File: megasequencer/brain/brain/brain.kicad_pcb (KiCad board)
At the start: 2 copper layers, 99.1 x 99.1 mm, 90 parts, among them J1 TOP, J2 BOTTOM, J3 Keyboard, J4 EURO_PWR_2x5, J5 ICSP, J6 TO_OUTPUTS, J7 FROM_OUTPUTS, J8 RIGHT, SW1 RST, U1 78L05, U2 ATmega328P-PU, U3 TL074, U4 TL072, U5 74HC595, U6 74HC595, U7 TL074, U8 TL074, Y1 Crystal

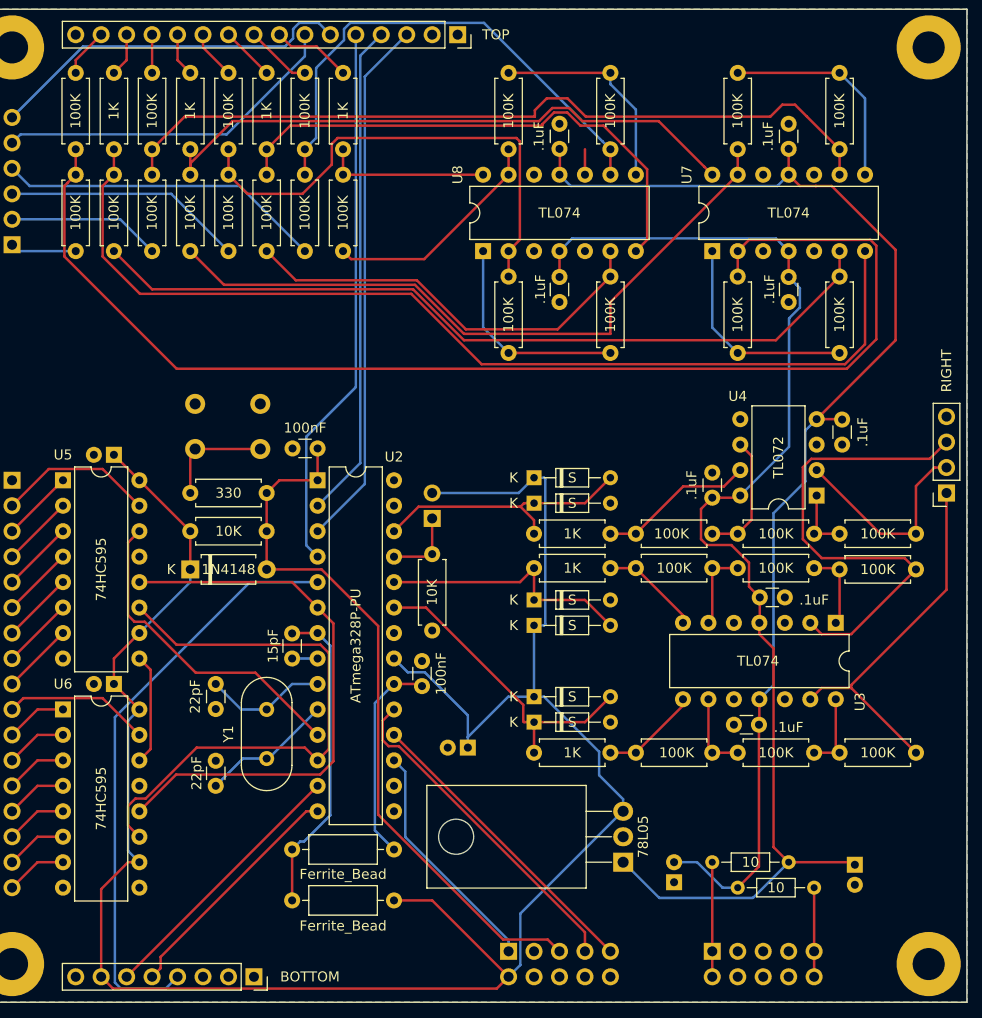
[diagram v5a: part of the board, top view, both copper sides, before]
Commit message: Finish up labeling and fixa connector that was in the wrong direction
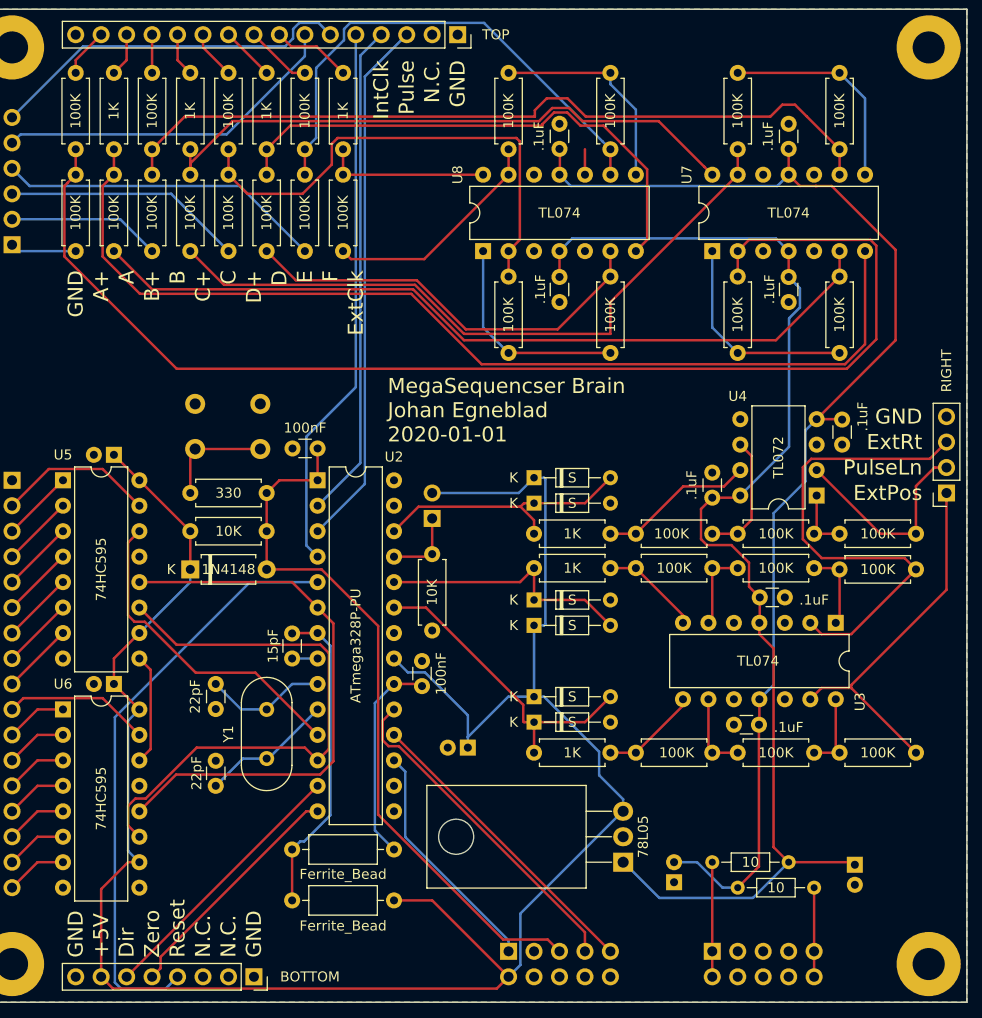
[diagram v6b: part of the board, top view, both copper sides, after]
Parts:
- J4: value EURO_PWR_2x5 -> POWER
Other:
- board text added: "+5V"
- board text added: "10"
- board text added: "11"
- board text added: "12"
- board text added: "13"
- board text added: "14"
- board text added: "15"
- board text added: "16"
- board text added: "2"
- board text added: "3"
- board text added: "4"
- board text added: "5"
- board text added: "6"
- board text added: "7"
- board text added: "8"
- board text added: "9"
- board text added: "A"
- board text added: "A+"
- board text added: "B"
- board text added: "B+"
- board text added: "C"
- board text added: "C+"
- board text added: "D"
- board text added: "D+"
- board text added: "Dir"
- board text added: "E"
- board text added: "ExtClk"
- board text added: "ExtPos"
- board text added: "ExtRt"
- board text added: "F"
- board text added: "G"
- board text added: "GND"
- board text added: "IntClk"
- board text added: "MegaSequencser Brain Johan Egneblad 2020-01-01"
- board text added: "N.C."
- board text added: "Pulse"
- board text added: "PulseLn"
- board text added: "Reset"
- board text added: "Zero"
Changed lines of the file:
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@@
   (general
     (thickness 1.6)
-    (drawings 7)
+    (drawings 59)
     (tracks 458)
     (zones 0)
@@
   (page A4)
   (layers
-    (0 F.Cu signal hide)
-    (31 B.Cu signal hide)
+    (0 F.Cu signal)
+    (31 B.Cu signal)
     (32 B.Adhes user)
     (33 F.Adhes user)
@@
       (effects (font (size 1 1) (thickness 0.15)) (justify mirror))
     )
-    (fp_text value EURO_PWR_2x5 (at -3.175 -6.35) (layer B.SilkS)
+    (fp_text value POWER (at -3.175 -9.525) (layer B.SilkS)
       (effects (font (size 1 1) (thickness 0.15)) (justify mirror))
     )
@@
       (effects (font (size 1 1) (thickness 0.15)))
     )
-    (fp_text value .1uF (at 1.25 2.05 90) (layer F.SilkS)
+    (fp_text value .1uF (at 2.794 2.05 90) (layer F.SilkS)
       (effects (font (size 1 1) (thickness 0.15)))
     )
@@
     )
   )
+  (gr_text 16 (at 31.115 113.03) (layer B.SilkS)
+    (effects (font (size 1 1) (thickness 0.15)) (justify right mirror))
+  )
+  (gr_text 15 (at 31.115 110.49) (layer B.SilkS)
+    (effects (font (size 1 1) (thickness 0.15)) (justify right mirror))
+  )
+  (gr_text 14 (at 31.115 107.95) (layer B.SilkS)
+    (effects (font (size 1 1) (thickness 0.15)) (justify right mirror))
+  )
+  (gr_text 13 (at 31.115 105.41) (layer B.SilkS)
+    (effects (font (size 1 1) (thickness 0.15)) (justify right mirror))
+  )
+  (gr_text 12 (at 31.115 102.87) (layer B.SilkS)
+    (effects (font (size 1 1) (thickness 0.15)) (justify right mirror))
+  )
+  (gr_text 11 (at 31.115 100.33) (layer B.SilkS)
+    (effects (font (size 1 1) (thickness 0.15)) (justify right mirror))
+  )
+  (gr_text 10 (at 31.115 97.79) (layer B.SilkS)
+    (effects (font (size 1 1) (thickness 0.15)) (justify right mirror))
+  )
+  (gr_text 9 (at 31.75 95.25) (layer B.SilkS)
+    (effects (font (size 1 1) (thickness 0.15)) (justify right mirror))
+  )
+  (gr_text 8 (at 31.75 92.71) (layer B.SilkS)
+    (effects (font (size 1 1) (thickness 0.15)) (justify right mirror))
+  )
+  (gr_text 7 (at 31.75 90.17) (layer B.SilkS)
+    (effects (font (size 1 1) (thickness 0.15)) (justify right mirror))
+  )
+  (gr_text 6 (at 31.75 87.63) (layer B.SilkS)
+    (effects (font (size 1 1) (thickness 0.15)) (justify right mirror))
+  )
+  (gr_text 5 (at 31.75 85.09) (layer B.SilkS)
+    (effects (font (size 1 1) (thickness 0.15)) (justify right mirror))
+  )
+  (gr_text 4 (at 31.75 82.55) (layer B.SilkS)
+    (effects (font (size 1 1) (thickness 0.15)) (justify right mirror))
+  )
+  (gr_text 3 (at 31.75 80.01) (layer B.SilkS)
+    (effects (font (size 1 1) (thickness 0.15)) (justify right mirror))
+  )
+  (gr_text 2 (at 31.75 77.47) (layer B.SilkS)
+    (effects (font (size 1 1) (thickness 0.15)) (justify right mirror))
+  )
+  (gr_text 1 (at 31.75 74.93) (layer B.SilkS)
+    (effects (font (size 1 1) (thickness 0.15)) (justify right mirror))
+  )
+  (gr_text G (at 31.75 72.39) (layer B.SilkS)
+    (effects (font (size 1 1) (thickness 0.15)) (justify right mirror))
+  )
+  (gr_text F (at 31.75 36.195) (layer B.SilkS)
+    (effects (font (size 1 1) (thickness 0.15)) (justify right mirror))
+  )
+  (gr_text E (at 31.75 38.735) (layer B.SilkS)
+    (effects (font (size 1 1) (thickness 0.15)) (justify right mirror))
+  )
+  (gr_text D (at 31.75 41.275) (layer B.SilkS)
+    (effects (font (size 1 1) (thickness 0.15)) (justify right mirror))
+  )
+  (gr_text C (at 31.75 43.815) (layer B.SilkS)
+    (effects (font (size 1 1) (thickness 0.15)) (justify right mirror))
+  )
+  (gr_text B (at 31.75 46.355) (layer B.SilkS)
+    (effects (font (size 1 1) (thickness 0.15)) (justify right mirror))
+  )
+  (gr_text A (at 31.75 48.895) (layer B.SilkS)
+    (effects (font (size 1 1) (thickness 0.15)) (justify right mirror))
+  )
+  (gr_text "MegaSequencser Brain\nJohan Egneblad\n2020-01-01" (at 66.675 65.405) (layer F.SilkS)
+    (effects (font (size 1.5 1.5) (thickness 0.3)) (justify left))
+  )
+  (gr_text GND (at 120.015 66.04) (layer F.SilkS)
+    (effects (font (size 1.5 1.5) (thickness 0.3)) (justify right))
+  )
+  (gr_text ExtRt (at 120.015 68.58) (layer F.SilkS)
+    (effects (font (size 1.5 1.5) (thickness 0.3)) (justify right))
+  )
+  (gr_text PulseLn (at 120.015 71.12) (layer F.SilkS)
+    (effects (font (size 1.5 1.5) (thickness 0.3)) (justify right))
+  )
+  (gr_text ExtPos (at 120.015 73.66) (layer F.SilkS)
+    (effects (font (size 1.5 1.5) (thickness 0.3)) (justify right))
+  )
+  (gr_text GND (at 53.34 120.015 90) (layer F.SilkS)
+    (effects (font (size 1.5 1.5) (thickness 0.3)) (justify left))
+  )
+  (gr_text N.C. (at 50.8 120.015 90) (layer F.SilkS)
+    (effects (font (size 1.5 1.5) (thickness 0.3)) (justify left))
+  )
+  (gr_text N.C. (at 48.26 120.015 90) (layer F.SilkS)
+    (effects (font (size 1.5 1.5) (thickness 0.3)) (justify left))
+  )
+  (gr_text Reset (at 45.72 120.015 90) (layer F.SilkS)
+    (effects (font (size 1.5 1.5) (thickness 0.3)) (justify left))
+  )
+  (gr_text Zero (at 43.18 120.015 90) (layer F.SilkS)
+    (effects (font (size 1.5 1.5) (thickness 0.3)) (justify left))
+  )
+  (gr_text Dir (at 40.64 120.015 90) (layer F.SilkS)
+    (effects (font (size 1.5 1.5) (thickness 0.3)) (justify left))
+  )
+  (gr_text +5V (at 38.1 120.015 90) (layer F.SilkS)
+    (effects (font (size 1.5 1.5) (thickness 0.3)) (justify left))
+  )
+  (gr_text GND (at 35.56 120.015 90) (layer F.SilkS)
+    (effects (font (size 1.5 1.5) (thickness 0.3)) (justify left))
+  )
+  (gr_text GND (at 73.66 30.48 90) (layer F.SilkS)
+    (effects (font (size 1.5 1.5) (thickness 0.3)) (justify right))
+  )
+  (gr_text N.C. (at 71.12 30.48 90) (layer F.SilkS)
+    (effects (font (size 1.5 1.5) (thickness 0.3)) (justify right))
+  )
+  (gr_text Pulse (at 68.58 30.48 90) (layer F.SilkS)
+    (effects (font (size 1.5 1.5) (thickness 0.3)) (justify right))
+  )
+  (gr_text IntClk (at 66.04 30.48 90) (layer F.SilkS)
+    (effects (font (size 1.5 1.5) (thickness 0.3)) (justify right))
+  )
+  (gr_text ExtClk (at 63.5 51.435 90) (layer F.SilkS)
+    (effects (font (size 1.5 1.5) (thickness 0.3)) (justify right))
+  )
+  (gr_text F (at 60.96 51.435 90) (layer F.SilkS)
+    (effects (font (size 1.5 1.5) (thickness 0.3)) (justify right))
+  )
+  (gr_text E (at 58.42 51.435 90) (layer F.SilkS)
+    (effects (font (size 1.5 1.5) (thickness 0.3)) (justify right))
+  )
+  (gr_text D (at 55.88 51.435 90) (layer F.SilkS)
+    (effects (font (size 1.5 1.5) (thickness 0.3)) (justify right))
+  )
+  (gr_text D+ (at 53.34 51.435 90) (layer F.SilkS)
+    (effects (font (size 1.5 1.5) (thickness 0.3)) (justify right))
+  )
+  (gr_text C (at 50.8 51.435 90) (layer F.SilkS)
+    (effects (font (size 1.5 1.5) (thickness 0.3)) (justify right))
+  )
+  (gr_text C+ (at 48.26 51.435 90) (layer F.SilkS)
+    (effects (font (size 1.5 1.5) (thickness 0.3)) (justify right))
+  )
+  (gr_text B (at 45.72 51.435 90) (layer F.SilkS)
+    (effects (font (size 1.5 1.5) (thickness 0.3)) (justify right))
+  )
+  (gr_text B+ (at 43.18 51.435 90) (layer F.SilkS)
+    (effects (font (size 1.5 1.5) (thickness 0.3)) (justify right))
+  )
+  (gr_text A (at 40.64 51.435 90) (layer F.SilkS)
+    (effects (font (size 1.5 1.5) (thickness 0.3)) (justify right))
+  )
+  (gr_text A+ (at 38.1 51.435 90) (layer F.SilkS)
+    (effects (font (size 1.5 1.5) (thickness 0.3)) (justify right))
+  )
+  (gr_text GND (at 35.56 51.435 90) (layer F.SilkS)
+    (effects (font (size 1.5 1.5) (thickness 0.3)) (justify right))
+  )
   (gr_text -12V (at 114.935 120.65 90) (layer B.SilkS)
     (effects (font (size 1 1) (thickness 0.2)) (justify mirror))
@@
   (segment (start 35.56 30.48) (end 35.56 31.75) (width 0.25) (layer F.Cu) (net 32) (status 20))
   (segment (start 38.1 27.94) (end 35.56 30.48) (width 0.25) (layer F.Cu) (net 32) (status 10))
-  (segment (start 40.64 30.48) (end 39.37 31.75) (width 0.25) (layer F.Cu) (net 93) (status 20))
-  (segment (start 40.64 27.94) (end 40.64 30.48) (width 0.25) (layer F.Cu) (net 93) (status 10))
   (segment (start 43.18 27.94) (end 43.18 31.75) (width 0.25) (layer F.Cu) (net 33) (status 30))
   (segment (start 45.72 30.48) (end 46.99 31.75) (width 0.25) (layer F.Cu) (net 34) (status 20))
@@
   (segment (start 46.99 73.66) (end 46.99 69.755) (width 0.25) (layer F.Cu) (net 92) (status 30))
   (segment (start 47.475 69.27) (end 53.975 69.27) (width 0.25) (layer F.Cu) (net 92) (status 30))
+  (segment (start 40.64 30.48) (end 39.37 31.75) (width 0.25) (layer F.Cu) (net 93) (status 20))
+  (segment (start 40.64 27.94) (end 40.64 30.48) (width 0.25) (layer F.Cu) (net 93) (status 10))
   (segment (start 109.964001 87.739001) (end 108.839 86.614) (width 0.25) (layer F.Cu) (net 95) (status 20))
   (segment (start 112.920999 87.739001) (end 109.964001 87.739001) (width 0.25) (layer F.Cu) (net 95))

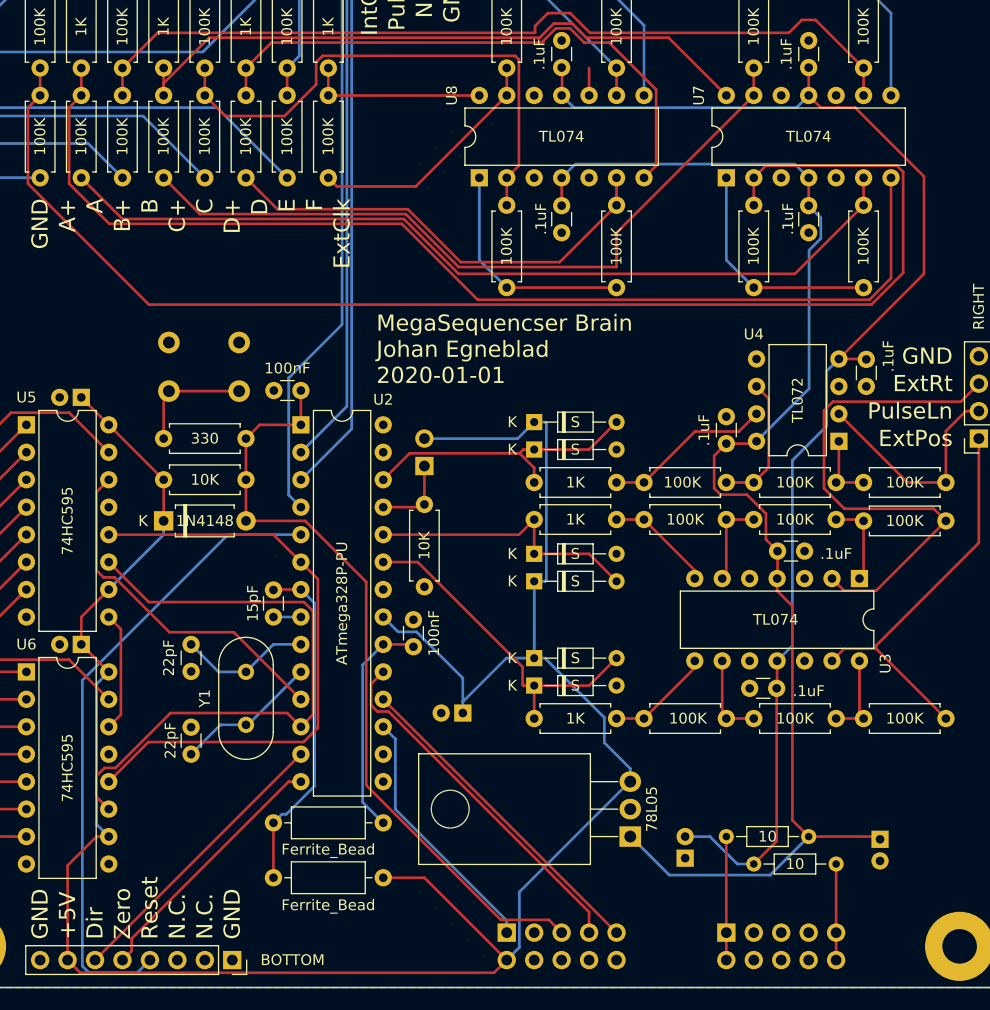
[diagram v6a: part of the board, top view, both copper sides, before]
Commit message: Increase trace width on brain, start sorting stuff for vco and start writing shopping list
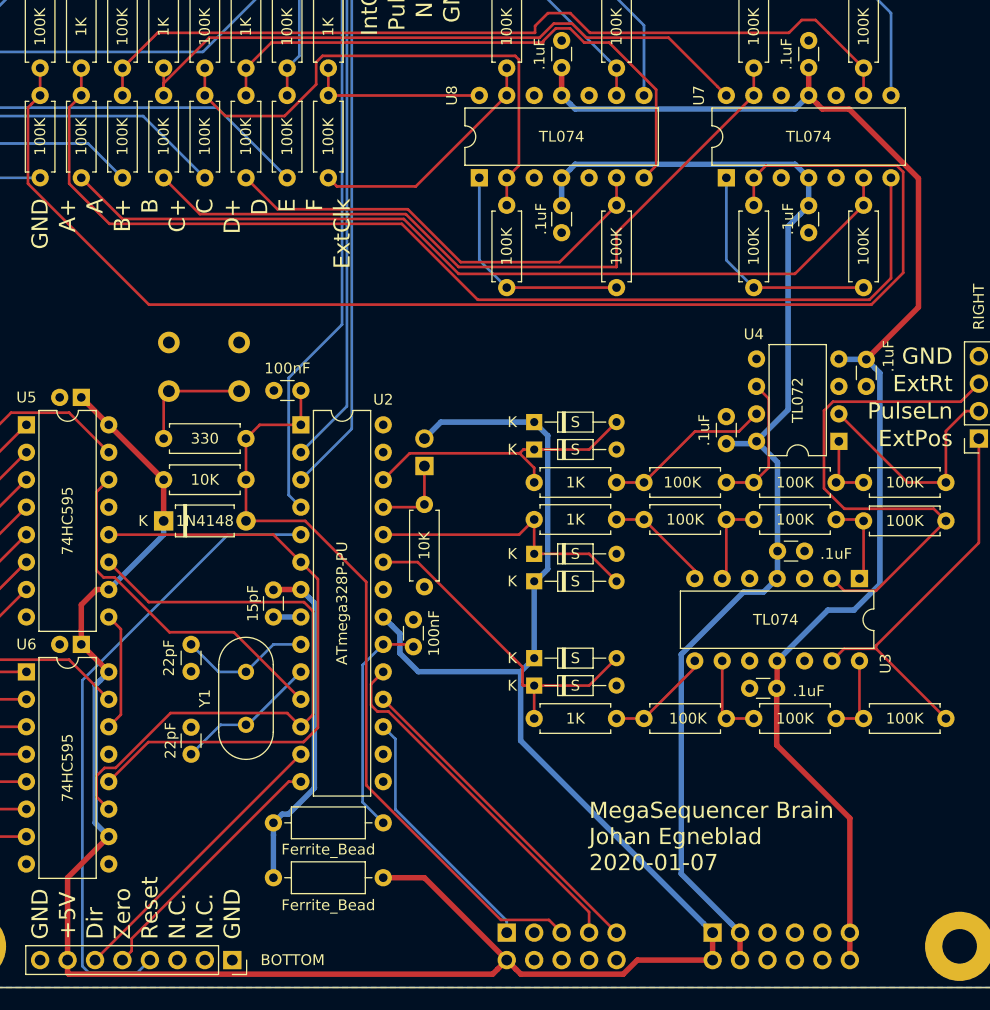
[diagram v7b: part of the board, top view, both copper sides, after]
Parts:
- removed C1, C2, C3: 10uF, Capacitor_THT:CP_Radial_D5.0mm_P2.00mm
- removed R2, R3: 10, Resistor_THT:R_Axial_DIN0204_L3.6mm_D1.6mm_P7.62mm_Horizontal
- removed U1: 78L05, Package_TO_SOT_THT:TO-220-3_Horizontal_TabDown
- J4: value POWER -> Filtered Power; footprint Connector_PinHeader_2.54mm:PinHeader_2x05_P2.54mm_Vertical -> Connector_PinHeader_2.54mm:PinHeader_2x06_P2.54mm_Vertical
- moved J4 1.27 mm to (97.8, 119.4)
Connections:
- J4 pad 1: Net-(J4-Pad1) -> +5V
- J4 pad 10: Net-(J4-Pad10) -> GND
- J4 pad 2: Net-(J4-Pad1) -> +5V
- J4 pad 3: GND -> +12V
- J4 pad 4: GND -> +12V
- J4 pad 9: Net-(J4-Pad10) -> GND
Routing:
- net +5V: track 211.7 -> 225.3 mm
- net +12V: track 124.7 -> 112.1 mm
- net Net-(J4-Pad1): track 11.4 -> 0.00 mm
- net Net-(J4-Pad10): track 8.89 -> 0.00 mm
- net -12V: track 122.9 -> 128.2 mm
- net GND: track 5.08 -> 2.54 mm
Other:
- net class Power added: clearance 0.2, trace_width 0.508, via_dia 0.8, via_drill 0.4
- board text added: "+12V"
- board text added: "MegaSequencer Brain Johan Egneblad 2020-01-07"
- board text removed: "MegaSequencser Brain Johan Egneblad 2020-01-01"
